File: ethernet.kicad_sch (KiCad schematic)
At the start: 34 parts, among them U1 MCIMX6Y2DVM09AB

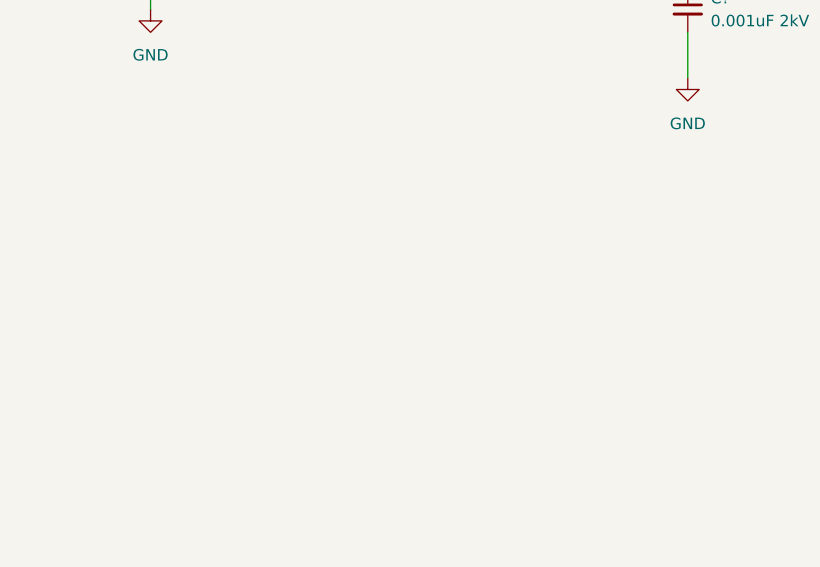
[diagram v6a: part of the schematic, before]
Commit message: Ethernet TVS, UART headers
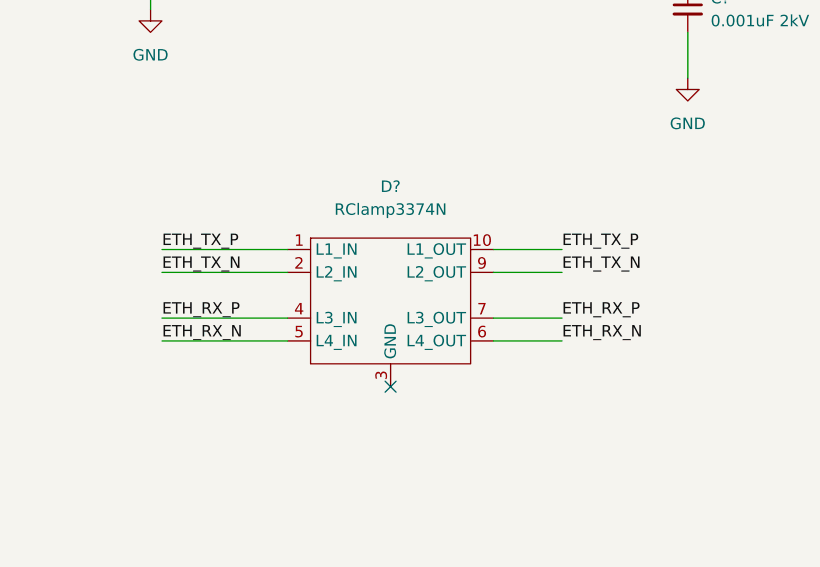
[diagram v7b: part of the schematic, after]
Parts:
- added D?: RClamp3374N, symbol catfood:RClamp3374N
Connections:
- net ETH_RX_N: now also D?.5 (L4_IN), D?.6 (L4_OUT)
- net ETH_RX_P: now also D?.4 (L3_IN), D?.7 (L3_OUT)
- net ETH_TX_N: now also D?.2 (L2_IN), D?.9 (L2_OUT)
- net ETH_TX_P: now also D?.1 (L1_IN), D?.10 (L1_OUT)
- net GND: now also D?.11 (GND), D?.12 (GND), D?.13 (GND), D?.3 (GND), D?.8 (GND)
- no-connect marks 18 -> 19
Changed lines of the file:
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@@
   (no_connect (at 66.04 156.21))
   (no_connect (at 66.04 148.59))
+  (no_connect (at 322.58 212.09))
   (no_connect (at 177.8 173.99))
   (no_connect (at 214.63 161.29))
@@
     (stroke (width 0) (type default) (color 0 0 0 0))
   )
+  (wire (pts (xy 334.01 207.01) (xy 341.63 207.01))
+    (stroke (width 0) (type default) (color 0 0 0 0))
+  )
   (wire (pts (xy 195.58 104.14) (xy 198.12 104.14))
     (stroke (width 0) (type default) (color 0 0 0 0))
@@
     (stroke (width 0) (type default) (color 0 0 0 0))
   )
+  (wire (pts (xy 297.18 199.39) (xy 311.15 199.39))
+    (stroke (width 0) (type default) (color 0 0 0 0))
+  )
   (wire (pts (xy 217.17 142.24) (xy 217.17 147.32))
     (stroke (width 0) (type default) (color 0 0 0 0))
@@
     (stroke (width 0) (type default) (color 0 0 0 0))
   )
+  (wire (pts (xy 334.01 196.85) (xy 341.63 196.85))
+    (stroke (width 0) (type default) (color 0 0 0 0))
+  )
   (wire (pts (xy 280.67 69.85) (xy 280.67 110.49))
     (stroke (width 0) (type default) (color 0 0 0 0))
@@
     (stroke (width 0) (type default) (color 0 0 0 0))
   )
+  (wire (pts (xy 334.01 204.47) (xy 341.63 204.47))
+    (stroke (width 0) (type default) (color 0 0 0 0))
+  )
   (wire (pts (xy 353.06 160.02) (xy 355.6 160.02))
     (stroke (width 0) (type default) (color 0 0 0 0))
   )
+  (wire (pts (xy 297.18 204.47) (xy 311.15 204.47))
+    (stroke (width 0) (type default) (color 0 0 0 0))
+  )
   (wire (pts (xy 353.06 152.4) (xy 355.6 152.4))
     (stroke (width 0) (type default) (color 0 0 0 0))
@@
     (stroke (width 0) (type default) (color 0 0 0 0))
   )
+  (wire (pts (xy 297.18 196.85) (xy 311.15 196.85))
+    (stroke (width 0) (type default) (color 0 0 0 0))
+  )
   (wire (pts (xy 82.55 158.75) (xy 82.55 124.46))
     (stroke (width 0) (type default) (color 0 0 0 0))
@@
     (stroke (width 0) (type default) (color 0 0 0 0))
   )
+  (wire (pts (xy 297.18 207.01) (xy 311.15 207.01))
+    (stroke (width 0) (type default) (color 0 0 0 0))
+  )
   (wire (pts (xy 355.6 160.02) (xy 355.6 167.64))
     (stroke (width 0) (type default) (color 0 0 0 0))
@@
     (stroke (width 0) (type default) (color 0 0 0 0))
   )
+  (wire (pts (xy 334.01 199.39) (xy 341.63 199.39))
+    (stroke (width 0) (type default) (color 0 0 0 0))
+  )
   (wire (pts (xy 295.91 161.29) (xy 295.91 142.24))
     (stroke (width 0) (type default) (color 0 0 0 0))
@@
     (effects (font (size 1.27 1.27)) (justify left bottom))
   )
+  (label "ETH_TX_N" (at 341.63 199.39 0)
+    (effects (font (size 1.27 1.27)) (justify left bottom))
+  )
   (label "LINKLED" (at 381 153.67 0)
     (effects (font (size 1.27 1.27)) (justify left bottom))
@@
     (effects (font (size 1.27 1.27)) (justify left bottom))
   )
+  (label "ETH_TX_P" (at 341.63 196.85 0)
+    (effects (font (size 1.27 1.27)) (justify left bottom))
+  )
   (label "ACTIVITYLED" (at 378.46 123.19 0)
     (effects (font (size 1.27 1.27)) (justify left bottom))
   )
+  (label "ETH_RX_P" (at 297.18 204.47 0)
+    (effects (font (size 1.27 1.27)) (justify left bottom))
+  )
   (label "ETH_TX_N" (at 255.27 133.35 0)
     (effects (font (size 1.27 1.27)) (justify left bottom))
@@
     (effects (font (size 1.27 1.27)) (justify left bottom))
   )
+  (label "ETH_TX_N" (at 297.18 199.39 0)
+    (effects (font (size 1.27 1.27)) (justify left bottom))
+  )
+  (label "ETH_RX_N" (at 297.18 207.01 0)
+    (effects (font (size 1.27 1.27)) (justify left bottom))
+  )
+  (label "ETH_TX_P" (at 297.18 196.85 0)
+    (effects (font (size 1.27 1.27)) (justify left bottom))
+  )
   (label "VETH_3V3" (at 161.29 69.85 0)
     (effects (font (size 1.27 1.27)) (justify left bottom))
@@
     (effects (font (size 1.27 1.27)) (justify left bottom))
   )
+  (label "ETH_RX_N" (at 341.63 207.01 0)
+    (effects (font (size 1.27 1.27)) (justify left bottom))
+  )
   (label "ENET_CRSDV" (at 107.95 144.78 0)
+    (effects (font (size 1.27 1.27)) (justify left bottom))
+  )
+  (label "ETH_RX_P" (at 341.63 204.47 0)
     (effects (font (size 1.27 1.27)) (justify left bottom))
   )
@@
     (pin "2")
   )
+  (symbol (lib_id "catfood:RClamp3374N") (at 331.47 201.93 0) (unit 1)
+    (in_bom yes) (on_board yes) (fields_autoplaced)
+    (property "Reference" "D?" (id 0) (at 322.58 189.865 0))
+    (property "Value" "RClamp3374N" (id 1) (at 322.58 192.405 0))
+    (property "Footprint" "" (id 2) (at 331.47 201.93 0)
+      (effects (font (size 1.27 1.27)) hide)
+    )
+    (property "Datasheet" "" (id 3) (at 331.47 201.93 0)
+      (effects (font (size 1.27 1.27)) hide)
+    )
+    (pin "1")
+    (pin "10")
+    (pin "11")
+    (pin "12")
+    (pin "13")
+    (pin "2")
+    (pin "3")
+    (pin "4")
+    (pin "5")
+    (pin "6")
+    (pin "7")
+    (pin "8")
+    (pin "9")
+  )
   (symbol (lib_id "Device:R_Small") (at 280.67 113.03 0) (unit 1)

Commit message: Annotation
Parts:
- gave numbers to parts that had none: 34
- renumbered U1 to U4
